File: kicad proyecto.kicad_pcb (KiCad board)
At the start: 4 copper layers, 100 x 100 mm, 46 parts, among them J1 USB_B, J2 UART, Q1 MMBT3904, SW1 SW_SPST, SW2 SW_SPST, SW3 SW_SPST, U1 NE555D, U2 NE555D, U3 FT232RL, U4 LM741, U5 4040, U6 4040

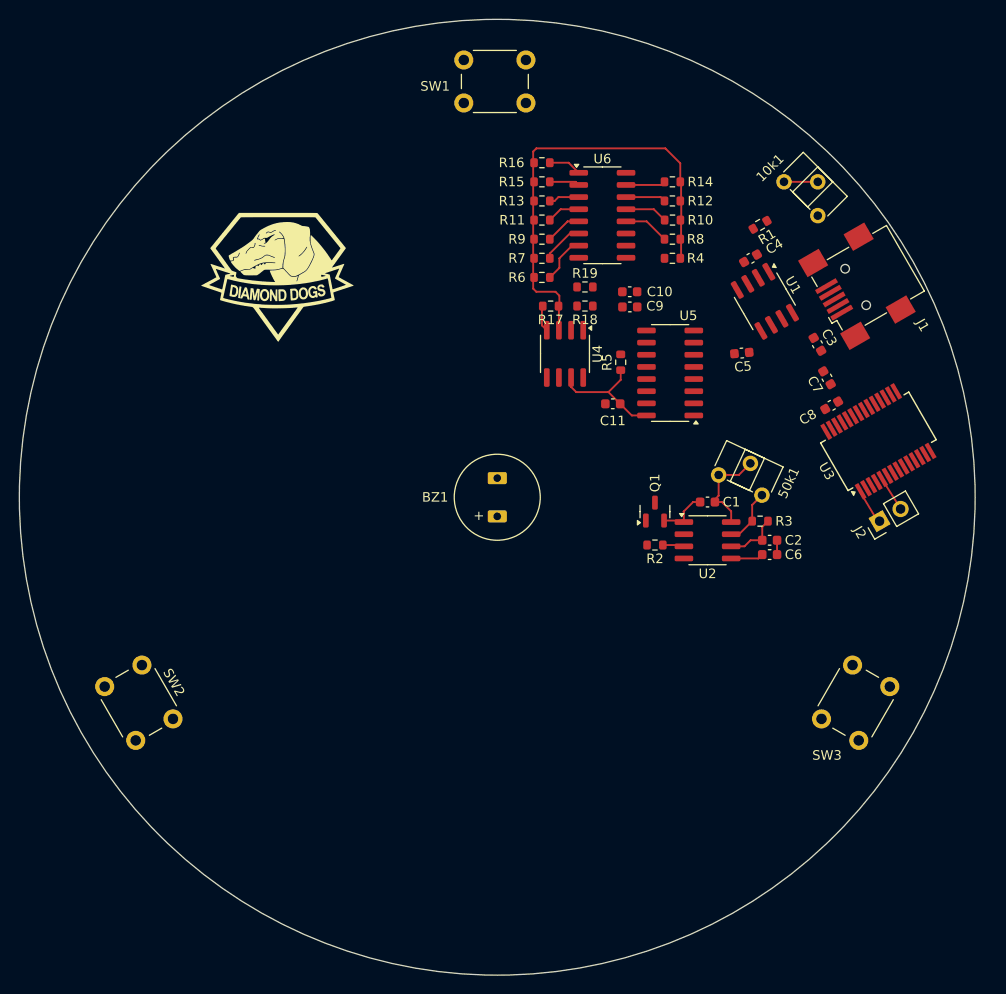
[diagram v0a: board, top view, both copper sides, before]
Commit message: Ruteo completo para baja frecuencia
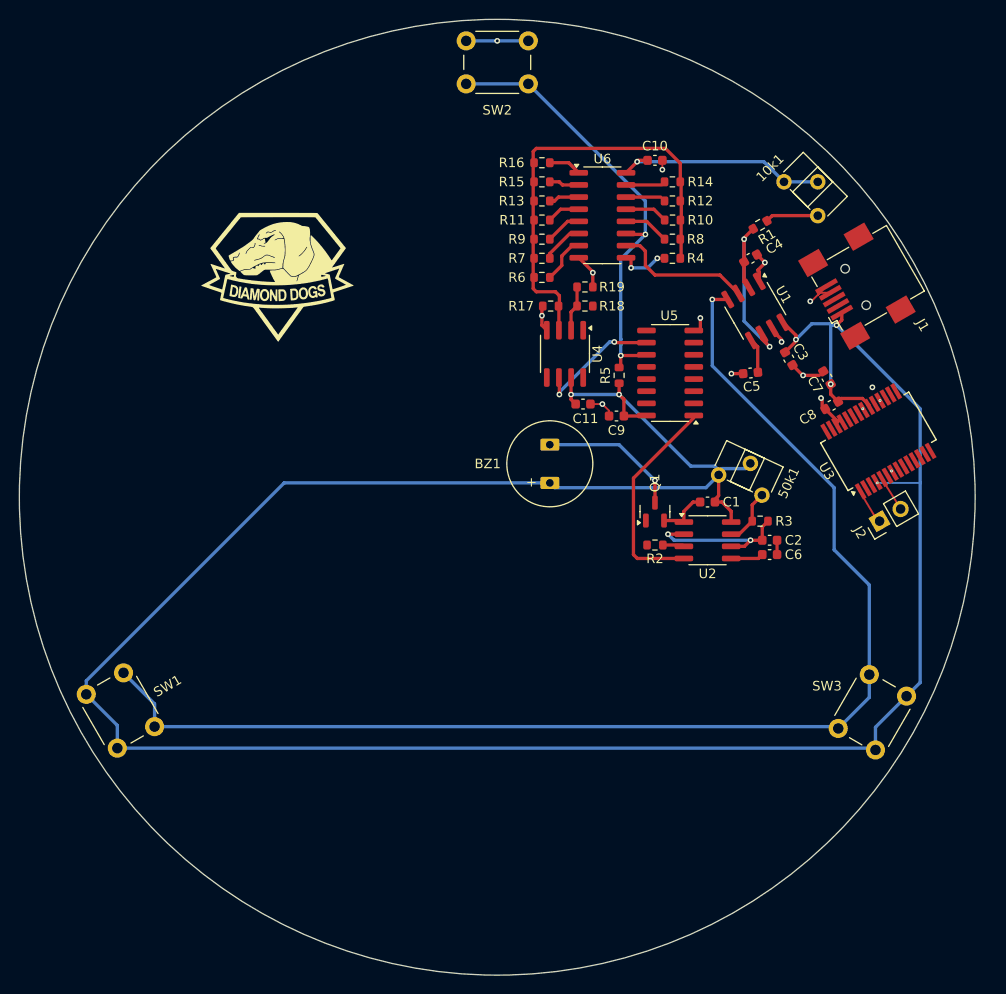
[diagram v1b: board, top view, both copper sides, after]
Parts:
- moved SW1 79.9 mm to (105.2, 131.2), turned to 120 degrees
- moved SW2 73.0 mm to (148.2, 61.8), turned to 180 degrees
- moved C10 14.0 mm to (161.5, 69.8), turned to 0 degrees
- moved C9 11.5 mm to (157.5, 96.5)
- moved SW3 9.21 mm to (187.8, 125.8), turned to -120 degrees
- moved BZ1 6.52 mm to (150.5, 101.5)
- moved C3 3.35 mm to (175.5, 90.5)
- moved C11 3.11 mm to (154.0, 95.3), turned to 0 degrees
- moved C5 2.28 mm to (171.5, 92.0)
- moved U1 1.41 mm to (172.0, 85.5)
- moved R5 1.38 mm to (157.8, 92.2)
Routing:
- net +5V: track 26.5 -> 302.0 mm, vias 0 -> 7
- net Net-(SW1-B): track 0.00 -> 133.4 mm, vias 0 -> 1
- net RESET: track 0.00 -> 47.2 mm, vias 0 -> 2
- net GND: track 9.62 -> 43.3 mm, vias 0 -> 14
- net /alarm: track 0.00 -> 22.6 mm
- net Net-(U1-THR): track 0.00 -> 20.8 mm, vias 0 -> 2
- net Net-(BZ1--): track 0.00 -> 14.9 mm, vias 0 -> 1
- net CLOCK: track 0.00 -> 14.7 mm
- net Net-(U5-CLK): track 0.00 -> 13.4 mm, vias 0 -> 2
- net Net-(U2-THR): track 5.76 -> 16.3 mm, vias 0 -> 2
- net Net-(U1-DIS): track 0.00 -> 7.37 mm, vias 0 -> 1
- net Net-(U6-Q0): track 0.00 -> 5.79 mm, vias 0 -> 2
- net Net-(U4--): track 0.00 -> 4.78 mm
- net Net-(U1-CV): track 0.00 -> 3.62 mm
- net (no net): vias 0 -> 1

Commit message: Add files via upload
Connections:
- net Net-(J1-D+) renamed /USB_D+
- net Net-(J1-D-) renamed /USB_D-
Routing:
- net Net-(U1-DIS): track 7.37 -> 20.7 mm, vias 1 -> 2
- net GND: track 43.3 -> 49.9 mm, vias 14 -> 17
- net /USB_D-: track 0.00 -> 4.37 mm
- net /USB_D+: track 0.00 -> 4.04 mm, vias 0 -> 2
- net +5V: track 302.0 -> 305.1 mm
- net (no net): vias 1 -> 0

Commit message: Add files via upload
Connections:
- net /USB_D+ renamed /USB_D P
- net /USB_D- renamed /USB_D N
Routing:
- net /USB_D P: track 4.04 -> 21.3 mm, vias 2 -> 0
- net /USB_D N: track 4.37 -> 17.2 mm

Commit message: REMapeo
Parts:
- moved J1 23.9 mm to (190.1, 105.7), turned to 90 degrees
- moved J2 18.2 mm to (190.3, 90.1), turned to 0 degrees
- moved C5 10.4 mm to (179.8, 85.9), turned to 0 degrees
- moved C3 9.51 mm to (179.8, 82.0), turned to 0 degrees
- moved C8 7.71 mm to (184.5, 101.6), turned to -90 degrees
- moved C7 7.40 mm to (173.2, 96.4), turned to 90 degrees
- moved U3 6.13 mm to (178.8, 99.9), turned to 0 degrees
- moved R1 4.21 mm to (169.9, 79.8), turned to -90 degrees
- moved C4 3.98 mm to (169.1, 83.2), turned to 180 degrees
- moved U1 3.06 mm to (174.6, 83.9), turned to 0 degrees
- moved 10k1 2.89 mm to (172.9, 70.0), turned to 0 degrees
- moved 50k1 2.88 mm to (165.3, 102.4), turned to 90 degrees
- moved C2 1.41 mm to (172.2, 110.1)
- moved C6 1.40 mm to (172.2, 111.6)
- moved C1 1.23 mm to (168.1, 105.9)
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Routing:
- net Net-(J2-Pin_1): track 0.00 -> 17.7 mm
- net Net-(J2-Pin_2): track 0.00 -> 17.5 mm
- net GND: track 49.9 -> 34.7 mm, vias 17 -> 21
- net +5V: track 305.1 -> 292.2 mm, vias 7 -> 10
- net /USB_D P: track 21.3 -> 9.32 mm
- net Net-(U1-THR): track 20.8 -> 10.3 mm, vias 2 -> 0
- net Net-(U2-THR): track 16.3 -> 9.66 mm, vias 2 -> 0
- net Net-(U1-DIS): track 20.7 -> 14.1 mm, vias 2 -> 0
- net /USB_D N: track 17.2 -> 10.8 mm
- net Net-(U2-DIS): track 5.91 -> 9.51 mm
- net Net-(SW1-B): track 133.4 -> 130.4 mm
- net Net-(Q1-B): track 0.00 -> 2.96 mm
- net CLOCK: track 14.7 -> 17.0 mm
- net Net-(U1-CV): track 3.62 -> 2.12 mm
- net Net-(U2-CV): track 3.42 -> 2.02 mm
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- added copper zone on B.Cu, net +5V
- added copper zone on In1.Cu, net GND
- added copper zone on In2.Cu, net GND
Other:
- board text added: "C7"

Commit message: Add files via upload
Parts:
- 10k1, 50k1: footprint Potentiometer_THT:Potentiometer_ACP_CA6-H2,5_Horizontal -> pretty:601030
- moved G*** 24.3 mm to (122.5, 106.3)
- moved 10k1 6.57 mm to (168.5, 74.9)
- moved C10 3.87 mm to (157.9, 68.4), turned to 180 degrees
- moved 50k1 3.35 mm to (168.5, 103.4)
- moved R4 2.50 mm to (162.1, 77.8)
- moved R6 2.18 mm to (150.0, 79.8)
- moved R8 2.07 mm to (162.1, 76.3)
- moved R7 1.70 mm to (150.0, 78.3)
- moved R10 1.69 mm to (162.1, 74.9)
- moved R12 1.36 mm to (162.1, 73.4)
- moved R14 1.23 mm to (162.1, 71.9)
- moved R9 1.16 mm to (150.0, 76.9)
- moved R16 1.07 mm to (150.0, 71.0)
- moved R11 0.67 mm to (150.0, 75.4)
- moved R15 0.60 mm to (150.0, 72.5)
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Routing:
- net +5V: track 292.2 -> 391.0 mm, vias 10 -> 14
- net Net-(U4-+): track 47.1 -> 40.8 mm
- net Net-(U2-DIS): track 9.51 -> 14.3 mm
- net GND: track 34.7 -> 37.7 mm, vias 21 -> 78
- net Net-(U6-Q8): track 4.80 -> 2.88 mm
- net Net-(U6-Q1): track 4.99 -> 3.19 mm
- net Net-(U6-Q7): track 4.51 -> 2.81 mm
- net Net-(U6-Q2): track 4.39 -> 3.09 mm
- net Net-(U6-Q9): track 4.19 -> 2.90 mm
- net Net-(U6-Q10): track 4.16 -> 2.98 mm
- net /USB_D P: track 9.32 -> 10.4 mm
- net Net-(U6-Q3): track 3.80 -> 3.01 mm
- net Net-(U6-Q11): track 3.46 -> 2.70 mm
- net Net-(J2-Pin_1): track 17.7 -> 17.0 mm
- net Net-(U6-Q0): track 5.79 -> 6.39 mm
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
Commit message: geber
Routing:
- net +5V: track 391.0 -> 383.2 mm, vias 14 -> 12
- net Net-(U5-CLK): track 12.7 -> 11.7 mm, vias 2 -> 0
- net Net-(SW1-B): track 130.4 -> 130.5 mm, vias 1 -> 0
- net GND: vias 78 -> 107

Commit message: Corregir gerber
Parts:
- moved SW2 0.42 mm to (148.2, 62.2)
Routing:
- net GND: track 37.7 -> 37.6 mm, vias 107 -> 72
